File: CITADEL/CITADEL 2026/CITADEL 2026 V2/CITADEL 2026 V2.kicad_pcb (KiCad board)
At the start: 2 copper layers, 141.5 x 109.7 mm, 72 parts, among them U1 ESP32-S3-DEVKITC-1-N8R8

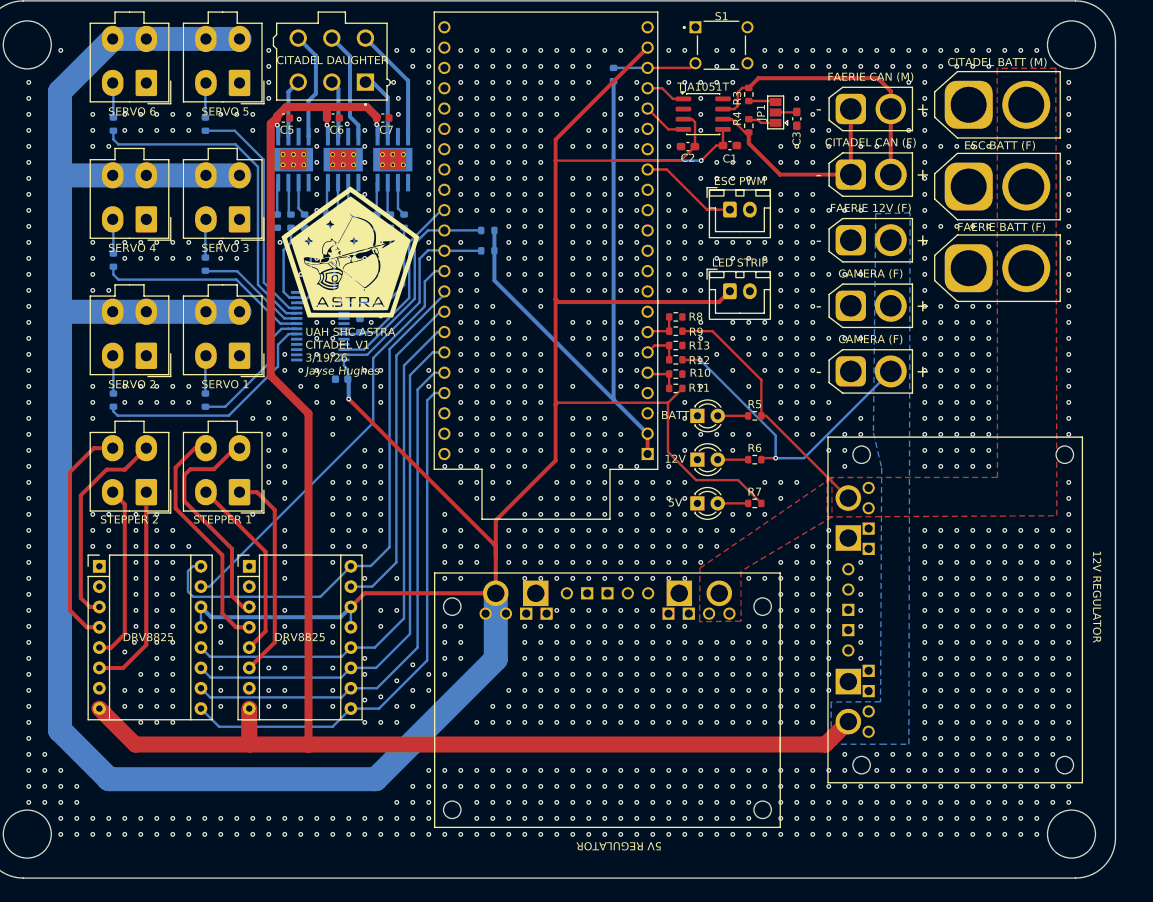
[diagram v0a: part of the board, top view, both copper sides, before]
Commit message: Removed steppers and updated silkscreen names
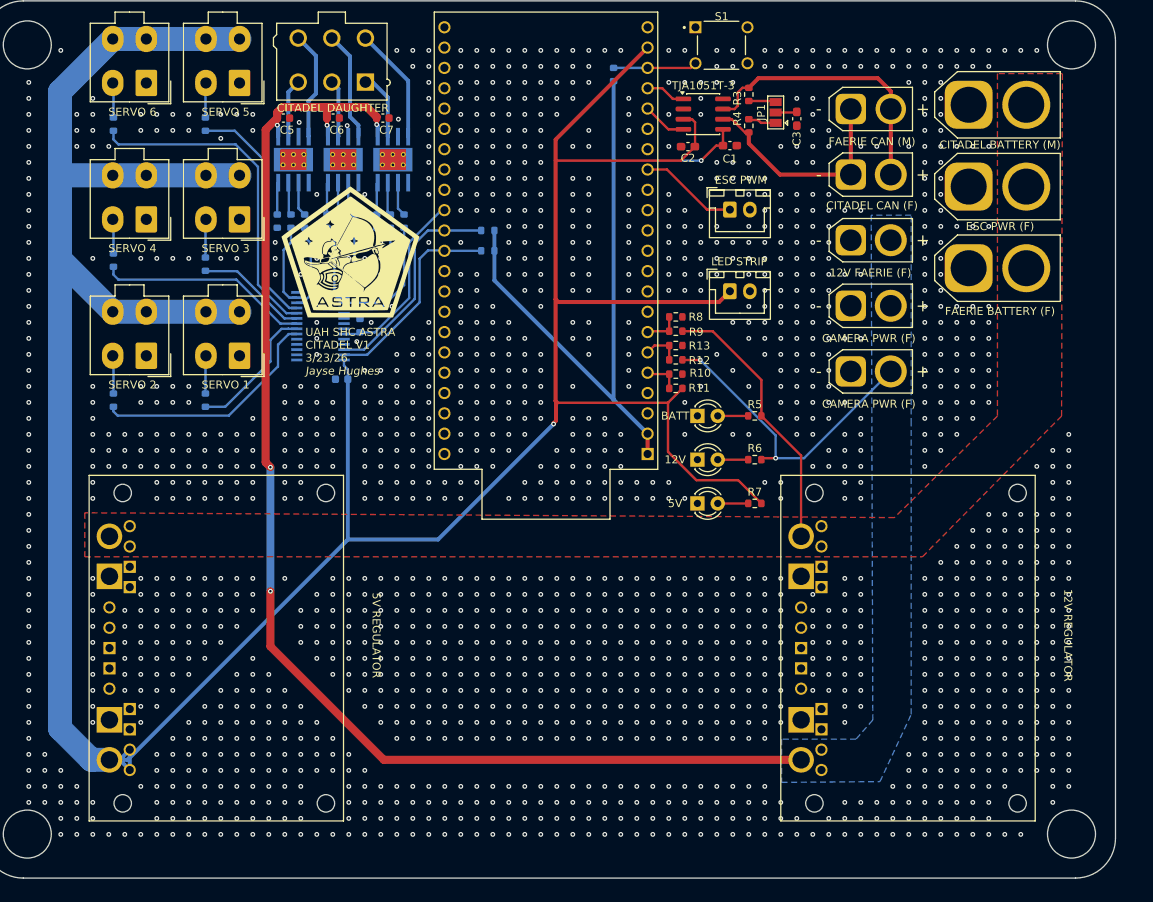
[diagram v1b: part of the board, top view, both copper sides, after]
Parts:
- removed A1, DRV8825: DRV8825, Module:Pololu_Breakout-16_15.2x20.3mm
- removed STEPPER 1: STEPPER 1, Connector_Molex:Molex_Mini-Fit_Jr_5566-04A_2x02_P4.20mm_Vertical
- removed STEPPER 2: STEPPER 2, Connector_Molex:Molex_Mini-Fit_Jr_5566-04A_2x02_P4.20mm_Vertical
- J1: renamed from FAERIE CAN (M)
- J10: renamed from ESC BATT (F)
- J13: renamed from CITADEL DAUGHTER
- J2: renamed from CITADEL CAN (F)
- J3: renamed from FAERIE 12V (F)
- J4: renamed from CITADEL BATT (M)
- J5: renamed from FAERIE BATT (F)
- J6: renamed from LED STRIP
- J7, J8: renamed from CAMERA (F)
- J9: renamed from ESC PWM
- M1: renamed from SERVO 1
- M2: renamed from SERVO 2
- M3: renamed from SERVO 3
- M4: renamed from SERVO 4
- M5: renamed from SERVO 5
- M6: renamed from SERVO 6
- Regulator1: renamed from 5V REGULATOR
- Regulator2: renamed from 12V REGULATOR
- moved Regulator1 41.5 mm to (70.4, 91.1), turned to -90 degrees
- moved Regulator2 7.59 mm to (156.9, 91.1)
- renumbered BATT to D1, 12V to D2, 5V to D3, TJA1051T to U2, PCA9685 to U3, DRV8871 to U4, DRV8871 to U5, DRV8871 to U6
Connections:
- U1 pad J3_10: /STEPPER2_STEP -> unconnected-(U1-GPIO38-PadJ3_10)
- U1 pad J3_4: /STEPPER_EN -> unconnected-(U1-GPIO1-PadJ3_4)
- U1 pad J3_5: /STEPPER_M0 -> unconnected-(U1-GPIO2-PadJ3_5)
- U1 pad J3_6: /STEPPER_M1 -> unconnected-(U1-MTMS/GPIO42-PadJ3_6)
- U1 pad J3_7: /STEPPER_M2 -> unconnected-(U1-MTDI/GPIO41-PadJ3_7)
- U1 pad J3_8: /STEPPER1_STEP -> unconnected-(U1-MTDO/GPIO40-PadJ3_8)
- U1 pad J3_9: /STEPPER_DIR -> unconnected-(U1-MTCK/GPIO39-PadJ3_9)
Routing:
- net /STEPPER_EN: track 67.7 -> 0.00 mm
- net /STEPPER_DIR: track 67.3 -> 0.00 mm
- net /STEPPER_M1: track 66.7 -> 0.00 mm
- net /STEPPER_M0: track 66.6 -> 0.00 mm
- net /STEPPER_M2: track 66.2 -> 0.00 mm
- net +5V: track 456.4 -> 397.6 mm
- net /STEPPER2_STEP: track 53.3 -> 0.00 mm
- net +12V: track 241.9 -> 200.6 mm, vias 5 -> 7
- net /STEPPER1_STEP: track 41.1 -> 0.00 mm
- net /MOTOR1_4: track 29.5 -> 0.00 mm
- net /MOTOR1_2: track 28.6 -> 0.00 mm
- net /MOTOR2_4: track 28.4 -> 0.00 mm
- net /MOTOR1_1: track 26.4 -> 0.00 mm
- net /MOTOR2_2: track 26.2 -> 0.00 mm
- net /MOTOR2_1: track 26.2 -> 0.00 mm
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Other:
- board text added: "UAH SHC ASTRA CITADEL V1 3/23/26"
- board text removed: "DRV8825"
- board text removed: "UAH SHC ASTRA CITADEL V1 3/19/26"
